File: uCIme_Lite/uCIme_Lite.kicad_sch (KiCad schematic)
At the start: 11 parts, among them J2 JACK-C-PC-10A-RA(R), J3 USB4081-03-A, J4 USB4081-03-A, J5 GPIO, J6 5V_ENABLE, J7 SERIAL, J8 JACK-C-PC-10A-RA(R), J9 USB4081-03-A

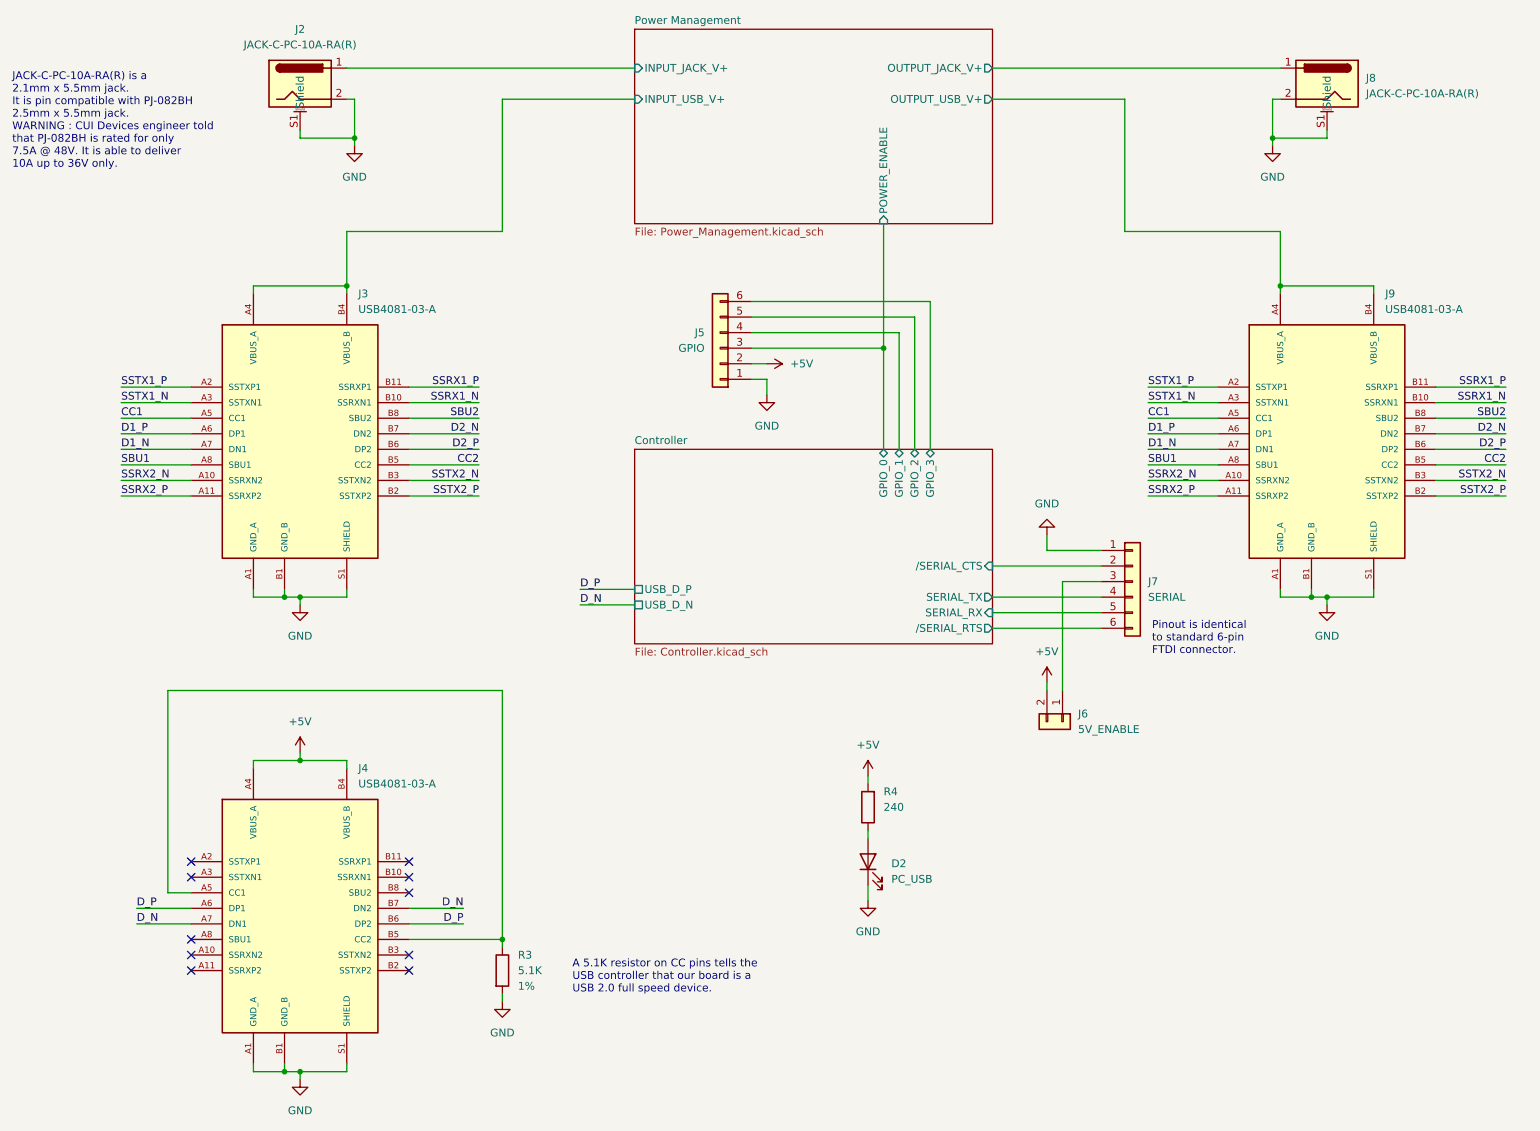
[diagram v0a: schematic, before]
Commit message: lite: Added more part numbers to the schematic. Replaced the FTDI 4.7u capacitor by two 2.2u capacitors to improve the BoM.
Signed-off-by: Adrien Ricciardi <aricciardi@baylibre.com>
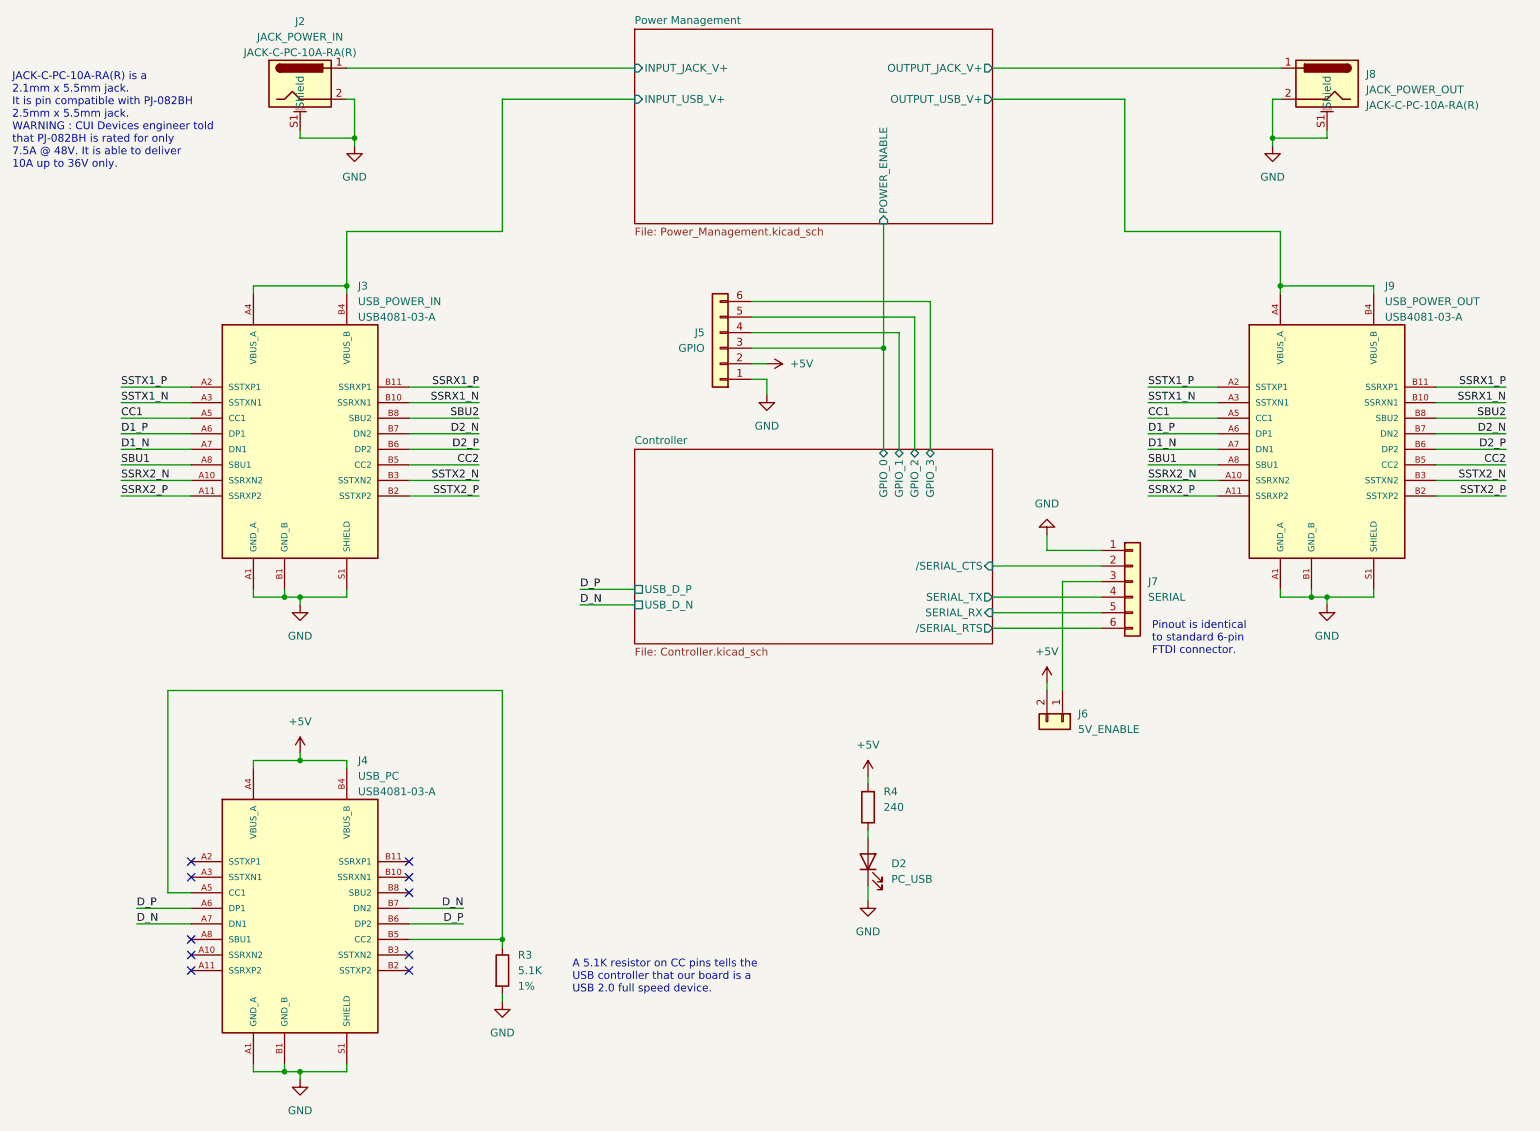
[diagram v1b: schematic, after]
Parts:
- J2: value JACK-C-PC-10A-RA(R) -> JACK_POWER_IN; PartNumber (none) -> JACK-C-PC-10A-RA(R)
- J3: value USB4081-03-A -> USB_POWER_IN
- J4: value USB4081-03-A -> USB_PC
- J8: value JACK-C-PC-10A-RA(R) -> JACK_POWER_OUT; PartNumber (none) -> JACK-C-PC-10A-RA(R)
- J9: value USB4081-03-A -> USB_POWER_OUT
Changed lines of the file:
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@@
   (symbol (lib_id "PJ-082BH:JACK-C-PC-10A-RA(R)") (at 229.87 26.67 0) (mirror y) (unit 1)
     (in_bom yes) (on_board yes) (dnp no) (fields_autoplaced)
-    (property "Reference" "J8" (at 236.22 25.7555 0)
+    (property "Reference" "J8" (at 236.22 25.1206 0)
       (effects (font (size 1.27 1.27)) (justify right))
     )
-    (property "Value" "JACK-C-PC-10A-RA(R)" (at 236.22 28.2955 0)
+    (property "Value" "JACK_POWER_OUT" (at 236.22 27.6606 0)
       (effects (font (size 1.27 1.27)) (justify right))
     )
@@
     (property "Datasheet" "" (at 229.87 26.67 0)
       (effects (font (size 1.27 1.27)) hide)
+    )
+    (property "PartNumber" "JACK-C-PC-10A-RA(R)" (at 236.22 30.2006 0)
+      (effects (font (size 1.27 1.27)) (justify right))
     )
     (pin "1")
@@
   (symbol (lib_id "PJ-082BH:JACK-C-PC-10A-RA(R)") (at 62.23 26.67 0) (unit 1)
     (in_bom yes) (on_board yes) (dnp no) (fields_autoplaced)
-    (property "Reference" "J2" (at 62.23 17.78 0)
-      (effects (font (size 1.27 1.27)))
-    )
-    (property "Value" "JACK-C-PC-10A-RA(R)" (at 62.23 20.32 0)
+    (property "Reference" "J2" (at 62.23 16.51 0)
+      (effects (font (size 1.27 1.27)))
+    )
+    (property "Value" "JACK_POWER_IN" (at 62.23 19.05 0)
       (effects (font (size 1.27 1.27)))
     )
@@
     (property "Datasheet" "" (at 62.23 26.67 0)
       (effects (font (size 1.27 1.27)) hide)
+    )
+    (property "PartNumber" "JACK-C-PC-10A-RA(R)" (at 62.23 21.59 0)
+      (effects (font (size 1.27 1.27)))
     )
     (pin "1")
@@
   (symbol (lib_id "USB4081:USB4081-03-A") (at 62.23 86.36 0) (unit 1)
     (in_bom yes) (on_board yes) (dnp no) (fields_autoplaced)
-    (property "Reference" "J3" (at 71.7297 60.96 0)
-      (effects (font (size 1.27 1.27)) (justify left))
-    )
-    (property "Value" "USB4081-03-A" (at 71.7297 63.5 0)
+    (property "Reference" "J3" (at 71.6789 59.69 0)
+      (effects (font (size 1.27 1.27)) (justify left))
+    )
+    (property "Value" "USB_POWER_IN" (at 71.6789 62.23 0)
       (effects (font (size 1.27 1.27)) (justify left))
     )
@@
       (effects (font (size 1.27 1.27)) hide)
     )
-    (property "PartNumber" "USB4081-03-A" (at 62.23 86.36 0)
-      (effects (font (size 1.27 1.27)) hide)
+    (property "PartNumber" "USB4081-03-A" (at 71.6789 64.77 0)
+      (effects (font (size 1.27 1.27)) (justify left))
     )
     (pin "A1")
@@
   (symbol (lib_id "USB4081:USB4081-03-A") (at 62.23 163.83 0) (unit 1)
     (in_bom yes) (on_board yes) (dnp no) (fields_autoplaced)
-    (property "Reference" "J4" (at 71.7297 138.43 0)
-      (effects (font (size 1.27 1.27)) (justify left))
-    )
-    (property "Value" "USB4081-03-A" (at 71.7297 140.97 0)
+    (property "Reference" "J4" (at 71.6789 137.16 0)
+      (effects (font (size 1.27 1.27)) (justify left))
+    )
+    (property "Value" "USB_PC" (at 71.6789 139.7 0)
       (effects (font (size 1.27 1.27)) (justify left))
     )
@@
       (effects (font (size 1.27 1.27)) hide)
     )
-    (property "PartNumber" "USB4081-03-A" (at 62.23 163.83 0)
-      (effects (font (size 1.27 1.27)) hide)
+    (property "PartNumber" "USB4081-03-A" (at 71.6789 142.24 0)
+      (effects (font (size 1.27 1.27)) (justify left))
     )
     (pin "A1")
@@
   (symbol (lib_id "USB4081:USB4081-03-A") (at 229.87 86.36 0) (unit 1)
     (in_bom yes) (on_board yes) (dnp no) (fields_autoplaced)
-    (property "Reference" "J9" (at 239.3697 60.96 0)
-      (effects (font (size 1.27 1.27)) (justify left))
-    )
-    (property "Value" "USB4081-03-A" (at 239.3697 63.5 0)
+    (property "Reference" "J9" (at 239.3189 59.69 0)
+      (effects (font (size 1.27 1.27)) (justify left))
+    )
+    (property "Value" "USB_POWER_OUT" (at 239.3189 62.23 0)
       (effects (font (size 1.27 1.27)) (justify left))
     )
@@
       (effects (font (size 1.27 1.27)) hide)
     )
-    (property "PartNumber" "USB4081-03-A" (at 229.87 86.36 0)
-      (effects (font (size 1.27 1.27)) hide)
+    (property "PartNumber" "USB4081-03-A" (at 239.3189 64.77 0)
+      (effects (font (size 1.27 1.27)) (justify left))
     )
     (pin "A1")

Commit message: lite: Added to schematic all missing part numbers but the pin header ones.
Signed-off-by: Adrien Ricciardi <aricciardi@baylibre.com>
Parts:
- D2: footprint (none) -> LED_SMD:LED_0805_2012Metric; PartNumber (none) -> 150080SS75000
- J5: footprint (none) -> Connector_PinHeader_2.54mm:PinHeader_1x06_P2.54mm_Horizontal
- R3: PartNumber (none) -> RC0603FR-075K1L
- R4: PartNumber (none) -> RC1206JR-07240RL
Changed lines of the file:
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@@
       (effects (font (size 1.27 1.27)) (justify right))
     )
-    (property "Footprint" "" (at 154.94 153.67 0)
+    (property "Footprint" "LED_SMD:LED_0805_2012Metric" (at 154.94 153.67 0)
       (effects (font (size 1.27 1.27)) hide)
     )
     (property "Datasheet" "~" (at 154.94 153.67 0)
+      (effects (font (size 1.27 1.27)) hide)
+    )
+    (property "PartNumber" "150080SS75000" (at 154.94 153.67 0)
       (effects (font (size 1.27 1.27)) hide)
     )
@@
     (property "Value2" "1%" (at 97.79 173.9899 0)
       (effects (font (size 1.27 1.27)) (justify left))
+    )
+    (property "PartNumber" "RC0603FR-075K1L" (at 95.25 171.45 0)
+      (effects (font (size 1.27 1.27)) hide)
     )
     (pin "1")
@@
       (effects (font (size 1.27 1.27)) hide)
     )
-    (property "PartNumber" "" (at 154.94 144.78 0)
+    (property "PartNumber" "RC1206JR-07240RL" (at 154.94 144.78 0)
       (effects (font (size 1.27 1.27)) hide)
     )
@@
       (effects (font (size 1.27 1.27)) (justify left))
     )
-    (property "Footprint" "" (at 130.81 69.85 0)
-      (effects (font (size 1.27 1.27)) hide)
-    )
+    (property "Footprint" "Connector_PinHeader_2.54mm:PinHeader_1x06_P2.54mm_Horizontal" (at 130.81 69.85 0)
+      (effects (font (size 1.27 1.27)) hide)
+    )
